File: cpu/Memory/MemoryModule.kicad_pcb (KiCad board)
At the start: 2 copper layers, 197.8 x 80 mm, 98 parts, among them J1 Interconnect, J2 Expansion Connector A, J3 Expansion Connector B, U1 AT28C64B-15PU, U10 AS6C6264-55PCN, U11 AS6C6264-55PCN, U12 AS6C6264-55PCN, U13 AS6C6264-55PCN, U14 AS6C6264-55PCN, U15 AS6C6264-55PCN, U16 AS6C6264-55PCN, U17 74LS173, U18 74LS139, U19 74LS139, U2 AT28C64B-15PU, U20 74LS04, U21 74LS08, U22 74LS08, U23 74LS08, U24 74LS245, U25 74LS245, U26 74LS245, U27 74LS245, U3 AT28C64B-15PU, U4 AT28C64B-15PU, U5 AS6C6264-55PCN, U6 AS6C6264-55PCN, U7 AS6C6264-55PCN, U8 AS6C6264-55PCN, U9 AS6C6264-55PCN

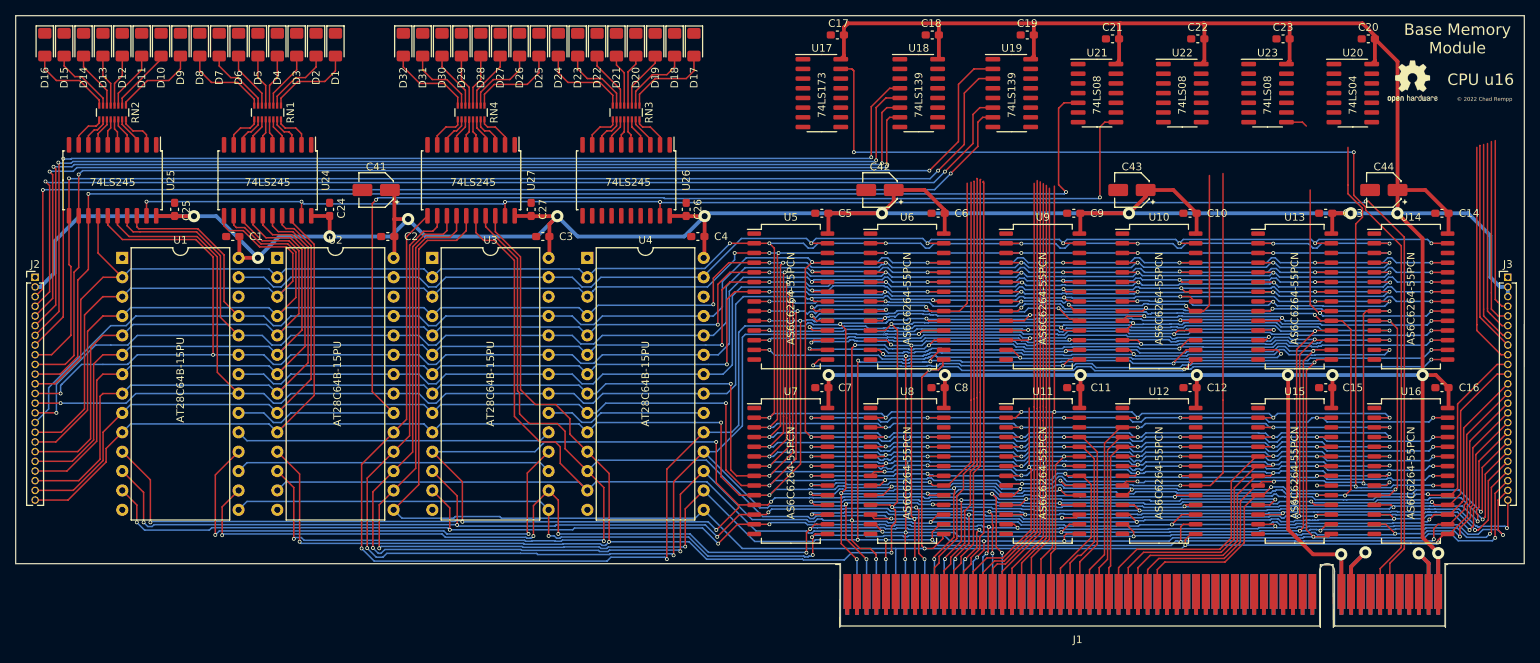
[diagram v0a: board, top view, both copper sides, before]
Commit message: Finished a draft of mem pcb
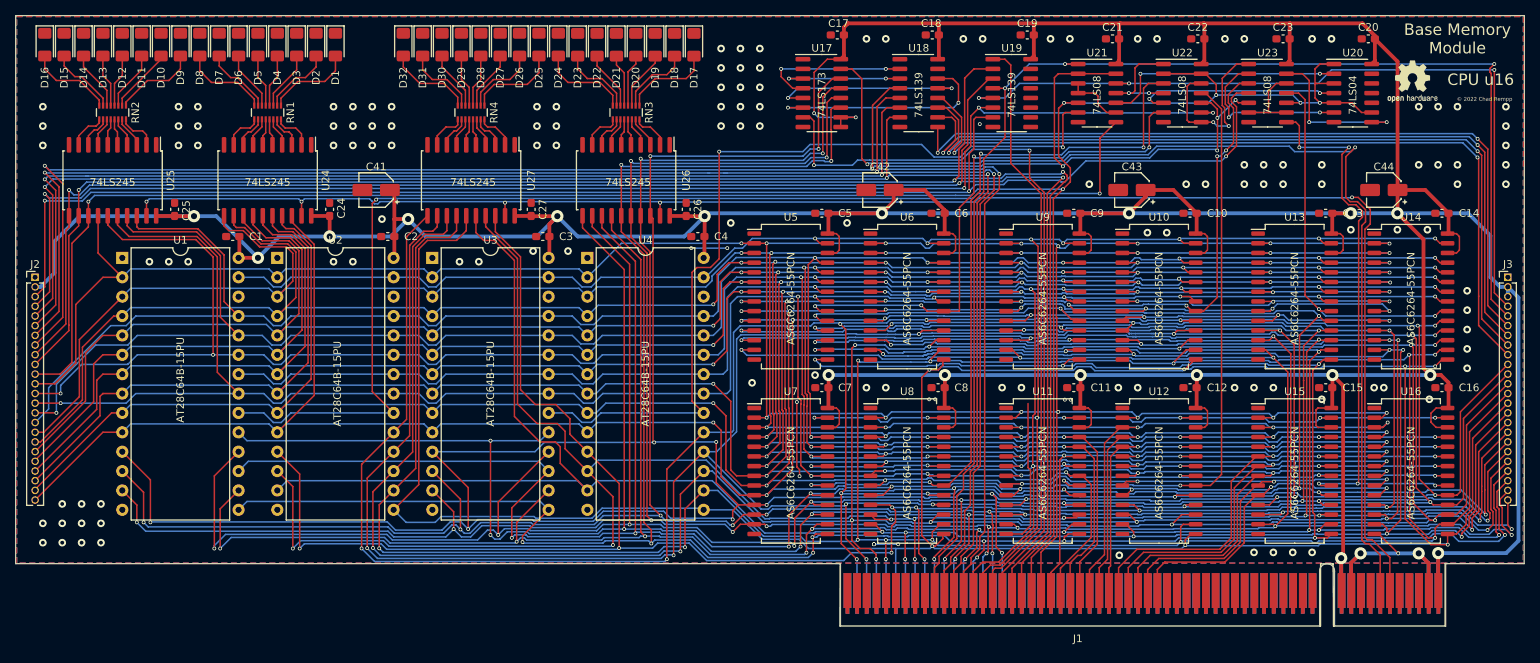
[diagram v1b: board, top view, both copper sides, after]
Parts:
- moved J1 0.13 mm to (197.5, 138.4)
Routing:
- net /md_bus_01: track 293.4 -> 407.1 mm, vias 12 -> 16
- net /md_bus_02: track 290.7 -> 401.3 mm, vias 12 -> 15
- net /md_bus_00: track 313.1 -> 417.8 mm, vias 12 -> 16
- net /md_bus_07: track 265.6 -> 366.8 mm, vias 10 -> 14
- net +5V: track 659.5 -> 758.5 mm, vias 19 -> 20
- net /md_bus_05: track 255.9 -> 352.8 mm, vias 10 -> 13
- net /md_bus_03: track 294.4 -> 387.7 mm, vias 11 -> 14
- net //bank_a_select: track 80.4 -> 172.8 mm, vias 0 -> 3
- net Net-(U4-Pad20): track 21.3 -> 111.9 mm, vias 0 -> 2
- net /md_bus_06: track 284.8 -> 373.6 mm, vias 12 -> 14
- net //enable_lowbank_0: track 143.4 -> 227.6 mm, vias 2 -> 6
- net //bank_b_select: track 22.8 -> 104.4 mm, vias 0 -> 3
- net //enable_highbank_2: track 26.7 -> 105.4 mm, vias 0 -> 2
- net //enable_highbank_1: track 27.7 -> 106.0 mm, vias 0 -> 2
- net //enable_highbank_0: track 29.4 -> 106.6 mm, vias 0 -> 2
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- added copper zone on B.Cu, net GND
- added copper zone on F.Cu, net GND

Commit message: Mem module fixes
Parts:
- removed REF**: OSHW-Logo2_7.3x6mm_SilkScreen, Symbol:OSHW-Logo2_7.3x6mm_SilkScreen
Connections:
- U21 pad 11: Net-(U21-Pad11) -> unconnected-(U21-Pad11)
- U21 pad 12: //bank_b_select -> unconnected-(U21-Pad12)
- U21 pad 13: //enable_lowbank_0 -> unconnected-(U21-Pad13)
- U22 pad 1: Net-(U21-Pad11) -> //bank_b_select
- U22 pad 10: //enable_lowbank_0 -> //enable_highbank_0
- U22 pad 4: Net-(U21-Pad11) -> //bank_b_select
- U23 pad 5: //enable_lowbank_0 -> //enable_highbank_0
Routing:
- net //enable_lowbank_0: track 227.6 -> 188.3 mm, vias 6 -> 3
- net Net-(U21-Pad11): track 14.1 -> 0.00 mm, vias 2 -> 0
- net //enable_highbank_0: track 106.6 -> 119.5 mm, vias 2 -> 5
- net GND: track 71.5 -> 78.8 mm, vias 145 -> 146
- net //bank_b_select: track 104.4 -> 111.1 mm, vias 3 -> 4
- net /RST: track 142.1 -> 138.1 mm
- net Net-(U15-Pad20): track 76.3 -> 78.9 mm, vias 5 -> 4
- net //bank_c_select: track 182.8 -> 183.9 mm
- net /~{DBG}: track 221.7 -> 220.5 mm
- net Net-(U22-Pad12): track 23.1 -> 22.1 mm
- net +5V: track 758.5 -> 757.7 mm
- net Net-(U11-Pad20): track 75.2 -> 75.8 mm
